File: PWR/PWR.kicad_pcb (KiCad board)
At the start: 2 copper layers, 71.6 x 70.1 mm, 20 parts, among them J1 +12v, P1 +5v, P2 GND, SW1 SPDT

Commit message: PCB layout...
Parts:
- added G***: LOGO, XS:Logo-XS-30mm, B.Cu at (134.1, 97.0)
- P1, P2: footprint XS:Connection-Molex-Breakaway-Header-Square-1x1 -> XS:Connection-Molex-Breakaway-Header-Square-1x1-Simple
- moved P1 1.02 mm to (161.0, 125.0)

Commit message: PCB edges.
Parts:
- moved C2 2.03 mm to (105.7, 124.5)
- moved C3 1.78 mm to (114.6, 124.5)
- moved G*** 1.02 mm to (128.0, 126.0)
- moved G*** 1.02 mm to (122.4, 126.0)
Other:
- board size 71.6 x 70.1 mm -> 70.1 x 65 mm
- board text added: "+5 volts power supply"
- board text added: "PWR rev1"
- board text removed: "PWR rev1 | +5 volts power supply"
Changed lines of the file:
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@@
     (links 26)
     (no_connects 26)
-    (area 99.009999 62.433999 170.738001 132.638001)
+    (area 100.025999 65.481999 170.230001 130.606001)
     (thickness 1.6)
-    (drawings 14)
+    (drawings 26)
     (tracks 0)
     (zones 0)
@@
   )
   (module XS:Logo-OWH (layer F.Cu)
-    (at 123.444 125.984)
+    (at 122.428 125.984)
     (fp_text reference G*** (at 0 0) (layer F.SilkS) hide
       (effects (font (thickness 0.3)))
@@
   )
   (module XS:Logo-XS (layer F.Cu)
-    (at 129.032 125.984)
+    (at 128.016 125.984)
     (fp_text reference G*** (at 0 0) (layer F.SilkS) hide
       (effects (font (thickness 0.3)))
@@
   )
   (module XS:Capacitor-Murata-RCE-Series-5mm (layer F.Cu)
-    (at 107.696 124.46 90)
+    (at 105.664 124.46 90)
     (fp_text reference C2 (at 0 3.556 90) (layer F.SilkS)
       (effects (font (size 1 1) (thickness 0.15)))
@@
   )
   (module XS:Capacitor-Murata-RCE-Series-5mm (layer F.Cu)
-    (at 116.332 124.46 90)
+    (at 114.554 124.46 90)
     (fp_text reference C3 (at 0 3.556 90) (layer F.SilkS)
       (effects (font (size 1 1) (thickness 0.15)))
@@
       (xy 14.986 -14.986)) (layer B.SilkS) (width 0.01))
   )
+  (gr_line (start 167.132 130.556) (end 103.124 130.556) (angle 90) (layer Edge.Cuts) (width 0.1))
+  (gr_line (start 170.18 127.508) (end 170.18 68.58) (angle 90) (layer Edge.Cuts) (width 0.1))
+  (gr_line (start 103.124 65.532) (end 167.132 65.532) (angle 90) (layer Edge.Cuts) (width 0.1))
+  (gr_line (start 100.076 127.508) (end 100.076 68.58) (angle 90) (layer Edge.Cuts) (width 0.1))
+  (gr_line (start 168.656 70.104) (end 168.656 97.536) (angle 90) (layer F.SilkS) (width 0.2))
+  (gr_line (start 164.592 70.104) (end 164.592 97.536) (angle 90) (layer F.SilkS) (width 0.2))
+  (gr_line (start 168.656 70.104) (end 164.592 70.104) (angle 90) (layer F.SilkS) (width 0.2))
+  (gr_text "+5 volts power supply" (at 166.624 84.074 90) (layer F.SilkS)
+    (effects (font (size 1.5 1.5) (thickness 0.3)))
+  )
+  (gr_line (start 164.592 109.728) (end 164.592 97.536) (angle 90) (layer F.SilkS) (width 0.2))
+  (gr_line (start 168.656 97.536) (end 168.656 109.728) (angle 90) (layer F.SilkS) (width 0.2))
+  (gr_line (start 164.592 97.536) (end 168.656 97.536) (angle 90) (layer F.SilkS) (width 0.2))
+  (gr_line (start 164.592 109.728) (end 168.656 109.728) (angle 90) (layer F.SilkS) (width 0.2))
+  (gr_line (start 152.4 122.936) (end 119.38 122.936) (angle 90) (layer F.SilkS) (width 0.2))
+  (gr_line (start 152.4 129.032) (end 152.4 122.936) (angle 90) (layer F.SilkS) (width 0.2))
+  (gr_line (start 119.38 129.032) (end 152.4 129.032) (angle 90) (layer F.SilkS) (width 0.2))
+  (gr_line (start 119.38 122.936) (end 119.38 129.032) (angle 90) (layer F.SilkS) (width 0.2))
   (gr_line (start 159.512 126.492) (end 159.512 123.444) (angle 90) (layer F.SilkS) (width 0.2))
   (gr_line (start 165.1 126.492) (end 159.512 126.492) (angle 90) (layer F.SilkS) (width 0.2))
   (gr_line (start 165.1 123.444) (end 165.1 126.492) (angle 90) (layer F.SilkS) (width 0.2))
   (gr_line (start 159.512 123.444) (end 165.1 123.444) (angle 90) (layer F.SilkS) (width 0.2))
-  (gr_text "PWR rev1 | +5 volts power supply" (at 166.624 109.474 90) (layer F.SilkS)
+  (gr_text "PWR rev1" (at 166.624 108.966 90) (layer F.SilkS)
     (effects (font (size 1.5 1.5) (thickness 0.3)) (justify left))
   )
-  (gr_line (start 99.06 65.532) (end 99.06 129.54) (angle 90) (layer Edge.Cuts) (width 0.1))
-  (gr_line (start 167.64 132.588) (end 102.108 132.588) (angle 90) (layer Edge.Cuts) (width 0.1))
-  (gr_line (start 170.688 65.532) (end 170.688 129.54) (angle 90) (layer Edge.Cuts) (width 0.1))
-  (gr_line (start 102.108 62.484) (end 167.64 62.484) (angle 90) (layer Edge.Cuts) (width 0.1))
-  (gr_arc (start 102.108 129.54) (end 102.108 132.588) (angle 90) (layer Edge.Cuts) (width 0.1))
-  (gr_arc (start 167.64 129.54) (end 170.688 129.54) (angle 90) (layer Edge.Cuts) (width 0.1))
-  (gr_arc (start 167.64 65.532) (end 167.64 62.484) (angle 90) (layer Edge.Cuts) (width 0.1))
-  (gr_arc (start 102.108 65.532) (end 99.06 65.532) (angle 90) (layer Edge.Cuts) (width 0.1))
-  (gr_text "XS-Labs © 2015\nwww.xs-labs.com" (at 132.334 125.984) (layer F.SilkS)
-    (effects (font (size 1.5 1.5) (thickness 0.3)) (justify left))
+  (gr_arc (start 103.124 127.508) (end 103.124 130.556) (angle 90) (layer Edge.Cuts) (width 0.1))
+  (gr_arc (start 167.132 127.508) (end 170.18 127.508) (angle 90) (layer Edge.Cuts) (width 0.1))
+  (gr_arc (start 167.132 68.58) (end 167.132 65.532) (angle 90) (layer Edge.Cuts) (width 0.1))
+  (gr_arc (start 103.124 68.58) (end 100.076 68.58) (angle 90) (layer Edge.Cuts) (width 0.1))
+  (gr_text "XS-Labs © 2015\nwww.xs-labs.com" (at 141.478 125.984) (layer F.SilkS)
+    (effects (font (size 1.5 1.5) (thickness 0.3)))
   )
 )

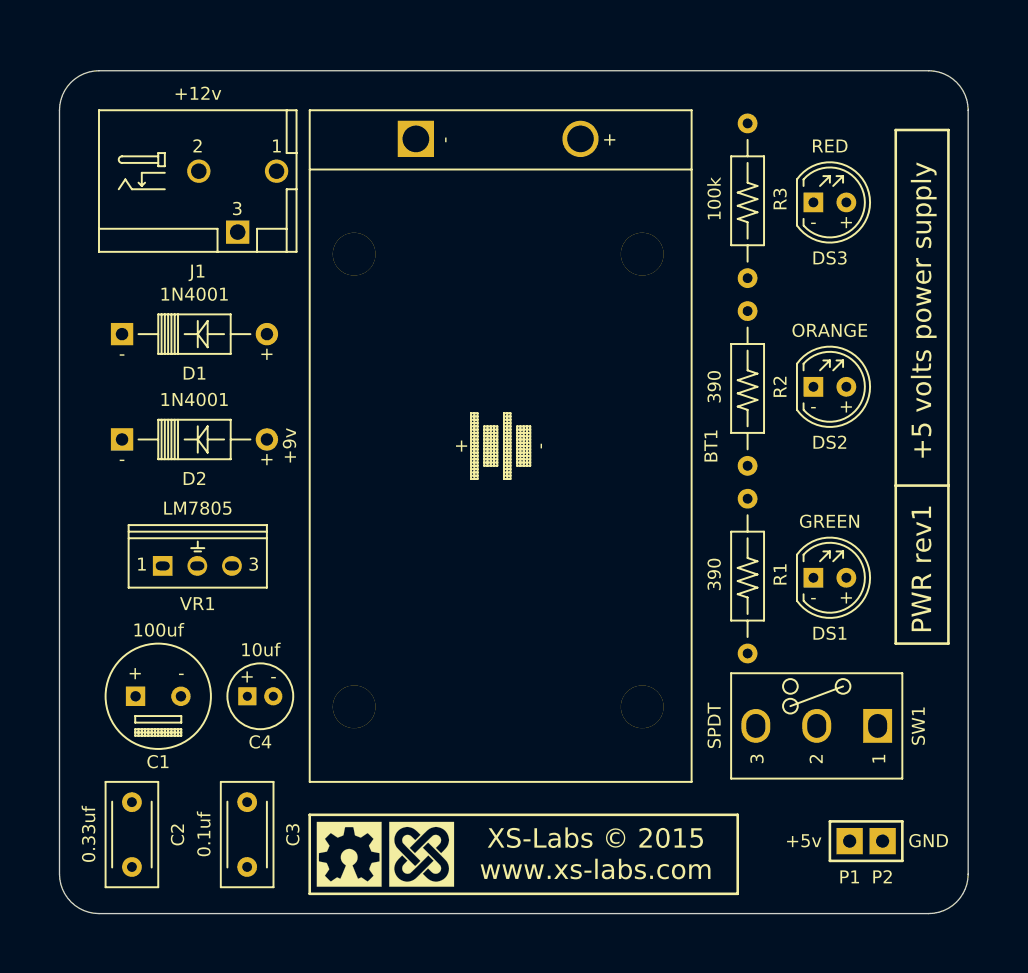
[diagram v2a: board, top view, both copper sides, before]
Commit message: Track width & clearance.
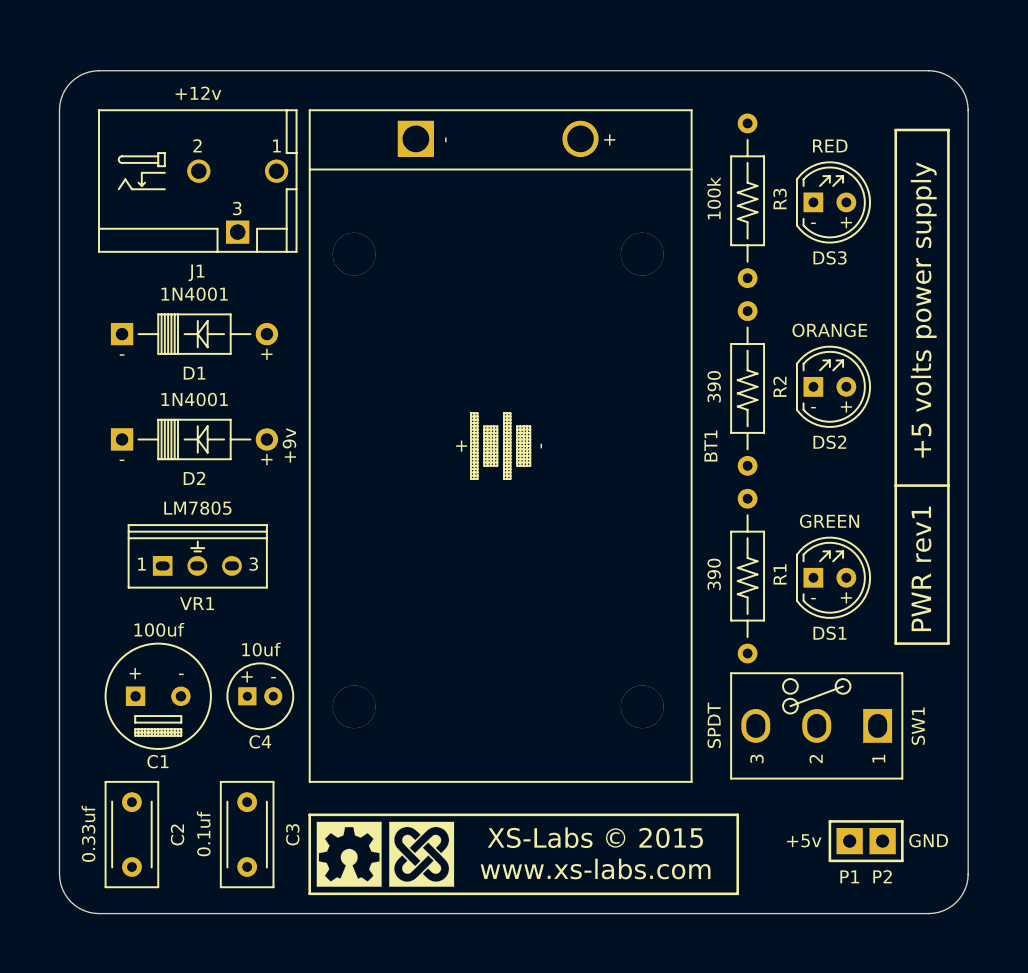
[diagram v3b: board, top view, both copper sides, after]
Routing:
- net Net-(J1-Pad2): track 0.00 -> 0.89 mm
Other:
- net class Default: clearance 0.2 -> 0.381; trace_width 0.25 -> 0.762; via_dia 0.6 -> 0.635; via_drill 0.4 -> 0.381
- rule trace_clearance: 0.2 -> 0.381
- rule trace_min: 0.2 -> 0.381
- rule via_min_drill: 0.3 -> 0.381
- rule via_min_size: 0.4 -> 0.635
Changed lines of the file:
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@@
     (thickness 1.6)
     (drawings 26)
-    (tracks 0)
+    (tracks 6)
     (zones 0)
     (modules 21)
@@
   )
   (setup
-    (last_trace_width 0.25)
-    (trace_clearance 0.2)
+    (last_trace_width 0.762)
+    (trace_clearance 0.381)
     (zone_clearance 0.508)
     (zone_45_only no)
-    (trace_min 0.2)
+    (trace_min 0.381)
     (segment_width 0.2)
     (edge_width 0.1)
-    (via_size 0.6)
-    (via_drill 0.4)
-    (via_min_size 0.4)
-    (via_min_drill 0.3)
+    (via_size 0.635)
+    (via_drill 0.381)
+    (via_min_size 0.635)
+    (via_min_drill 0.381)
     (uvia_size 0.3)
     (uvia_drill 0.1)
@@
   (net 11 "Net-(R3-Pad1)")
   (net_class Default "This is the default net class."
-    (clearance 0.2)
-    (trace_width 0.25)
-    (via_dia 0.6)
-    (via_drill 0.4)
+    (clearance 0.381)
+    (trace_width 0.762)
+    (via_dia 0.635)
+    (via_drill 0.381)
     (uvia_dia 0.3)
     (uvia_drill 0.1)
@@
     (effects (font (size 1.5 1.5) (thickness 0.3)))
   )
+  (segment (start 105.946 121.678) (end 105.664 121.96) (width 0.762) (layer B.Cu) (net 3) (status 30))
+  (segment (start 109.446 113.792) (end 109.474 113.792) (width 0.762) (layer B.Cu) (net 4) (status 30))
+  (segment (start 153.162 110.49) (end 153.162 110.744) (width 0.762) (layer B.Cu) (net 4) (status 30))
+  (segment (start 114.57 121.944) (end 114.554 121.96) (width 0.762) (layer B.Cu) (net 5) (status 30))
+  (segment (start 160.782 75.692) (end 160.782 75.946) (width 0.762) (layer B.Cu) (net 6) (status 30))
+  (segment (start 153.797 115.189) (end 153.797 116.078) (width 0.762) (layer B.Cu) (net 10) (status 30))
 )

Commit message: Routing...
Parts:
- moved P1 1.02 mm to (161.0, 126.0)
- moved P2 1.02 mm to (163.6, 126.0)
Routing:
- net Net-(C1-Pad2): track 0.28 -> 129.8 mm
- net Net-(D1-Pad2): track 0.25 -> 96.3 mm
- net Net-(J1-Pad2): track 0.89 -> 83.0 mm
- net Net-(BT1-Pad1): track 0.00 -> 74.0 mm, vias 0 -> 1
- net Net-(C3-Pad1): track 0.02 -> 66.5 mm, vias 0 -> 1
- net Net-(R3-Pad1): track 0.00 -> 46.9 mm, vias 0 -> 2
- net Net-(C1-Pad1): track 0.40 -> 38.8 mm
- net Net-(BT1-Pad2): track 0.00 -> 11.8 mm
- net Net-(DS3-Pad1): track 0.00 -> 10.4 mm
- net Net-(DS1-Pad1): track 0.00 -> 10.4 mm
- net Net-(DS2-Pad1): track 0.00 -> 10.2 mm
- net (no net): track 0.00 -> 0.51 mm
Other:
- board text added: "Off / On"

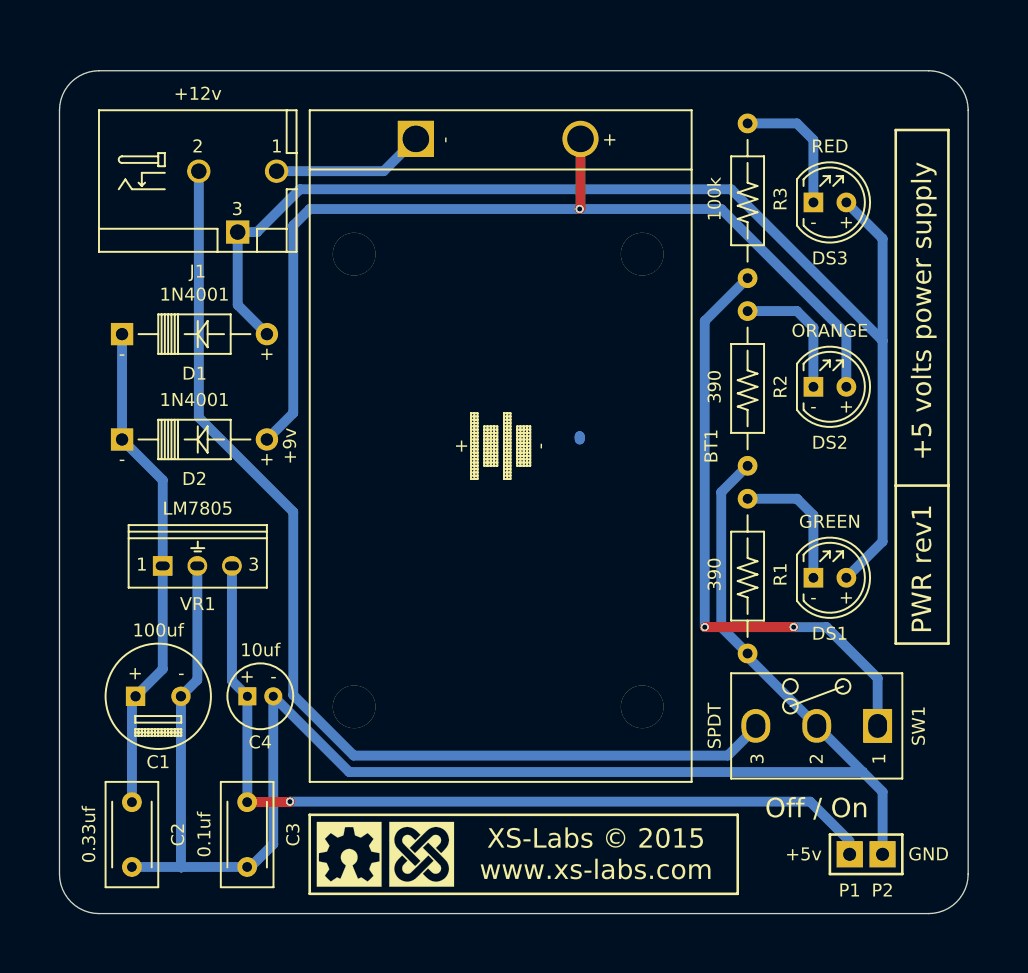
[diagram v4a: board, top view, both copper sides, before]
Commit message: Fixed pad numbers on Adafruit DC barrel jack.
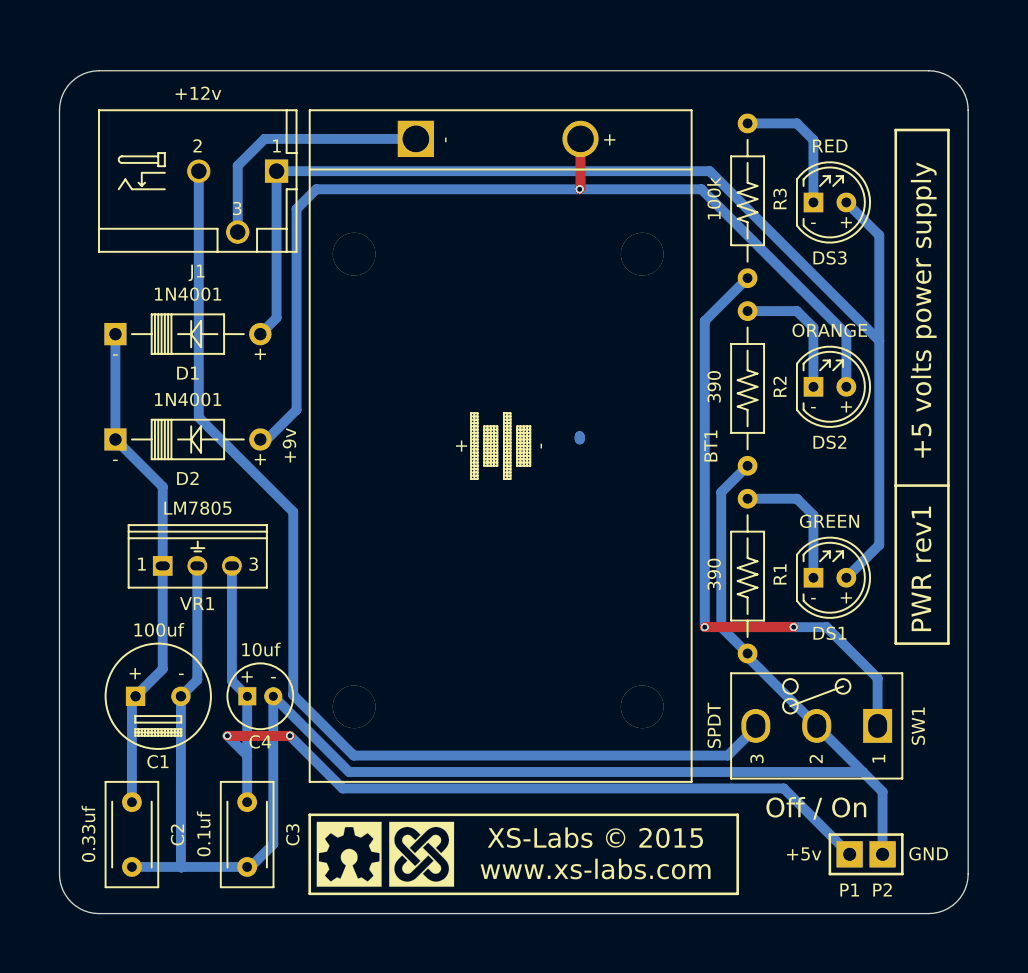
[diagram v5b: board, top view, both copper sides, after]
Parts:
- moved D1 0.51 mm to (110.0, 85.9)
- moved D2 0.51 mm to (110.0, 94.0)
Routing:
- net Net-(BT1-Pad2): track 11.8 -> 19.7 mm
- net Net-(C3-Pad1): track 66.5 -> 72.9 mm, vias 1 -> 2

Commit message: Cleanup...
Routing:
- net (no net): track 0.51 -> 0.00 mm

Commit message: Cleanup...
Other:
- board size 70.1 x 65 mm -> 75.2 x 70.1 mm
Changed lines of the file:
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@@
     (links 26)
     (no_connects 0)
-    (area 100.025999 65.481999 170.230001 130.606001)
+    (area 97.485999 62.941999 172.770001 133.146001)
     (thickness 1.6)
-    (drawings 27)
+    (drawings 35)
     (tracks 93)
     (zones 0)
@@
     (zone_45_only no)
     (trace_min 0.381)
-    (segment_width 0.2)
+    (segment_width 0.1)
     (edge_width 0.1)
     (via_size 0.635)
@@
       (net 6 "Net-(D1-Pad2)"))
   )
+  (gr_line (start 103.124 62.992) (end 167.132 62.992) (angle 90) (layer Edge.Cuts) (width 0.1))
+  (gr_line (start 97.536 127.508) (end 97.536 68.58) (angle 90) (layer Edge.Cuts) (width 0.1))
+  (gr_line (start 167.132 133.096) (end 103.124 133.096) (angle 90) (layer Edge.Cuts) (width 0.1))
+  (gr_line (start 172.72 68.58) (end 172.72 127.508) (angle 90) (layer Edge.Cuts) (width 0.1))
+  (gr_arc (start 167.132 68.58) (end 167.132 62.992) (angle 90) (layer Edge.Cuts) (width 0.1))
+  (gr_arc (start 167.132 127.508) (end 172.72 127.508) (angle 90) (layer Edge.Cuts) (width 0.1))
+  (gr_arc (start 103.124 127.508) (end 103.124 133.096) (angle 90) (layer Edge.Cuts) (width 0.1))
+  (gr_arc (start 103.124 68.58) (end 97.536 68.58) (angle 90) (layer Edge.Cuts) (width 0.1))
   (gr_text "Off / On" (at 158.496 122.428) (layer F.SilkS)
     (effects (font (size 1.5 1.5) (thickness 0.3)))
   )
-  (gr_line (start 167.132 130.556) (end 103.124 130.556) (angle 90) (layer Edge.Cuts) (width 0.1))
-  (gr_line (start 170.18 127.508) (end 170.18 68.58) (angle 90) (layer Edge.Cuts) (width 0.1))
-  (gr_line (start 103.124 65.532) (end 167.132 65.532) (angle 90) (layer Edge.Cuts) (width 0.1))
-  (gr_line (start 100.076 127.508) (end 100.076 68.58) (angle 90) (layer Edge.Cuts) (width 0.1))
+  (gr_line (start 167.132 130.556) (end 103.124 130.556) (angle 90) (layer F.SilkS) (width 0.1))
+  (gr_line (start 170.18 127.508) (end 170.18 68.58) (angle 90) (layer F.SilkS) (width 0.1))
+  (gr_line (start 103.124 65.532) (end 167.132 65.532) (angle 90) (layer F.SilkS) (width 0.1))
+  (gr_line (start 100.076 127.508) (end 100.076 68.58) (angle 90) (layer F.SilkS) (width 0.1))
   (gr_line (start 168.656 70.104) (end 168.656 97.536) (angle 90) (layer F.SilkS) (width 0.2))
   (gr_line (start 164.592 70.104) (end 164.592 97.536) (angle 90) (layer F.SilkS) (width 0.2))
@@
     (effects (font (size 1.5 1.5) (thickness 0.3)) (justify left))
   )
-  (gr_arc (start 103.124 127.508) (end 103.124 130.556) (angle 90) (layer Edge.Cuts) (width 0.1))
-  (gr_arc (start 167.132 127.508) (end 170.18 127.508) (angle 90) (layer Edge.Cuts) (width 0.1))
-  (gr_arc (start 167.132 68.58) (end 167.132 65.532) (angle 90) (layer Edge.Cuts) (width 0.1))
-  (gr_arc (start 103.124 68.58) (end 100.076 68.58) (angle 90) (layer Edge.Cuts) (width 0.1))
+  (gr_arc (start 103.124 127.508) (end 103.124 130.556) (angle 90) (layer F.SilkS) (width 0.1))
+  (gr_arc (start 167.132 127.508) (end 170.18 127.508) (angle 90) (layer F.SilkS) (width 0.1))
+  (gr_arc (start 167.132 68.58) (end 167.132 65.532) (angle 90) (layer F.SilkS) (width 0.1))
+  (gr_arc (start 103.124 68.58) (end 100.076 68.58) (angle 90) (layer F.SilkS) (width 0.1))
   (gr_text "XS-Labs © 2015\nwww.xs-labs.com" (at 141.478 125.984) (layer F.SilkS)
     (effects (font (size 1.5 1.5) (thickness 0.3)))

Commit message: Inverted logo...
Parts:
- moved G*** 0.25 mm to (134.1, 97.3)
